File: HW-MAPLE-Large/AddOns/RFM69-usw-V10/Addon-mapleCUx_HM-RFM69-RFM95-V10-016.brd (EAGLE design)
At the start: 49 x 47 mm, 35 parts, among them IC1 ATSHA204A, IC31 ATMEGA168-TQFP, X31 M03X2, X4 1751248, X7 1751264, Y2 8MHZ

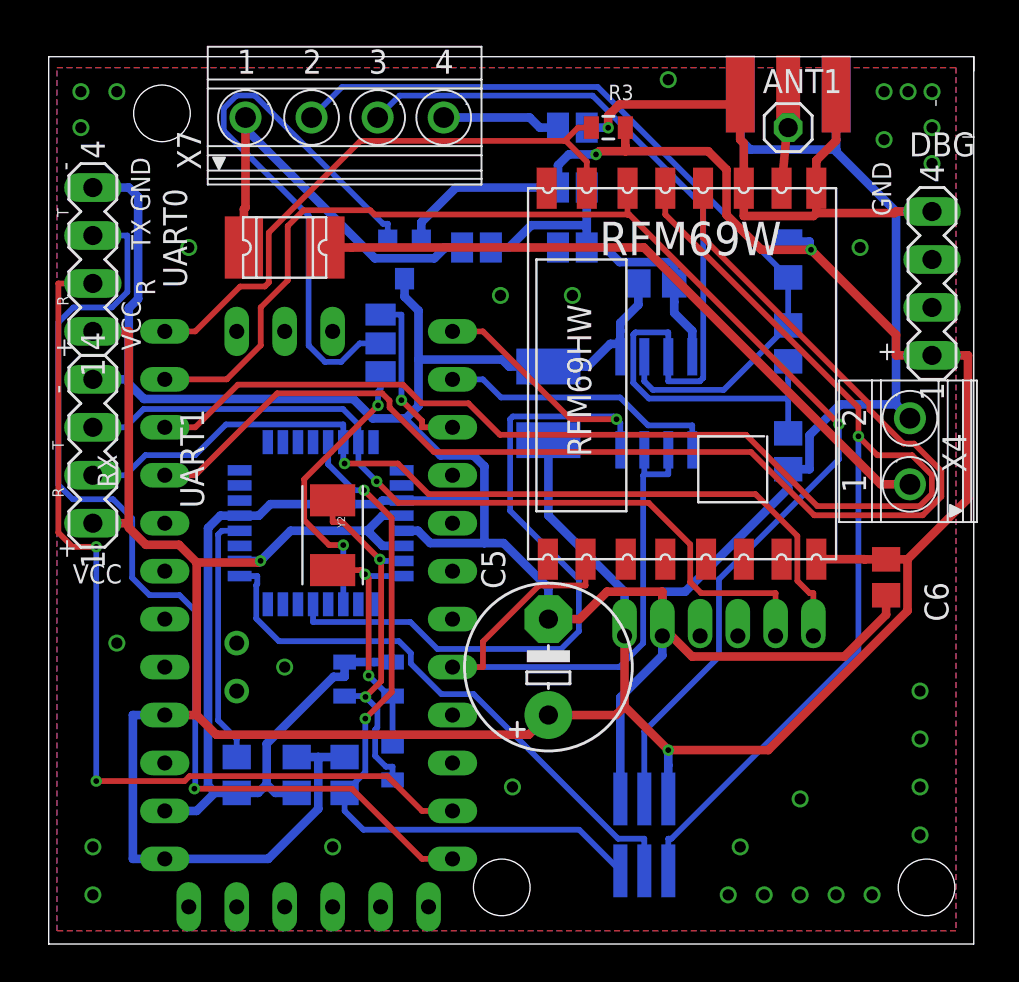
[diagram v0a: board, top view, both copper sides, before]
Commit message: Addon: plus RFM95
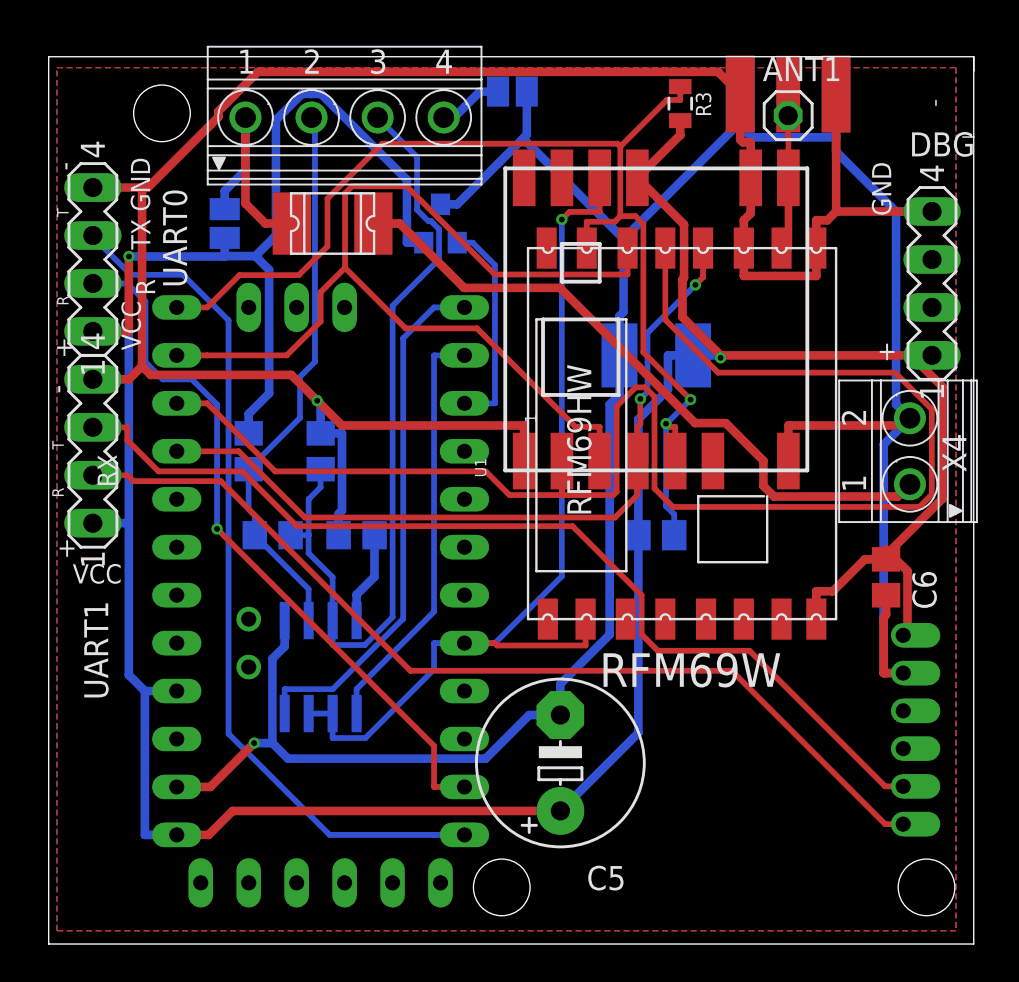
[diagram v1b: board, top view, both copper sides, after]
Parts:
- removed 3V3, 5V: (no value), jumper:SJ
- removed C14, C15: 30pf, doug:0805
- removed C31, C32: 100n, rcl:C0805
- removed IC31: ATMEGA168-TQFP, atmel:TQFP32-08
- removed R34: (no value), rcl:R0805
- removed R4: 1M, doug:0805
- removed SJ1: (no value), jumper:SJ_2
- removed X31: M03X2, mechanics:2X03-1.27MM_SMD
- removed Y2: 8MHZ, SparkFun-FreqCtrl:CRYSTAL-TXC-7A
- added R2: 10k, rcl:M0805
- added U1: RFM69HCW, doug:RFM69HCW-XXXS2
- moved R9 30.3 mm to (61.6, 38.1)
- moved R1 29.1 mm to (62.9, 33.7), turned to 180 degrees
- moved R10 24.8 mm to (65.4, 38.1), turned to 90 degrees
- moved RS1 22.6 mm to (65.4, 26.7)
- moved C10 20.7 mm to (67.3, 33.7)
- moved EXT 13.4 mm to (60.3, 50.2), turned to 90 degrees
- moved HMMOD-UART 12.3 mm to (96.3, 16.4), turned to 0 degrees
- moved C7 6.25 mm to (83.2, 43.2), turned to 180 degrees
- moved C5 5.12 mm to (78.1, 21.6)
- moved R3 4.02 mm to (84.5, 56.5), turned to 270 degrees
- moved GND 3.70 mm to (75.6, 57.1)
- moved RFM69W 3.17 mm to (92.7, 29.2)
- moved F1 2.84 mm to (66.0, 50.2)
- moved IC1 2.69 mm to (71.8, 50.2), turned to 0 degrees
- moved U$2 1.42 mm to (67.9, 24.1)
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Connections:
- removed net +5V: 5V.2
- removed net D10_SS: IC31.14
- removed net D11_MOSI: IC31.15
- removed net D12_MISO: IC31.16
- removed net D13_SCK: IC31.17, X31.P$3
- removed net D2_INT0: IC31.32
- removed net D7-ATSHA-MEGA: IC31.11, SJ1.1
- removed net M-RES: IC31.29, R34.2, X31.P$5
- removed net N$1: ANT1.1, RFM69W.ANT, X2.P
- removed net N$13: C32.1, IC31.20
- removed net N$19: C15.2, IC31.8, R4.1, Y2.P$1
- removed net N$3: C14.2, IC31.7, R4.2, Y2.P$2
- removed net N$5: IC1.1, SJ1.2
- new net ANT: ANT1.1, RFM69W.ANT, U1.ANT, X2.P
- new net N$14: U1.DIO2
- new net N$15: U1.DIO1
- new net N$2: U1.RESET
- net CE-A: no longer IC31.13
- net CSN-A: now also R2.1, U1.NSS
- net D7-ATSHA-ARDU: now also IC1.1; no longer SJ1.3
- net GND: now also U1.GND_1, U1.GND_2, U1.GND_3; no longer C14.1, C15.1, C31.2, C32.2, IC31.21, IC31.3, IC31.5, X31.P$6
- net IRQ-A: now also U1.DIO0
- net MISO-A: now also U1.MISO; no longer X31.P$1
- net MOSI-A: now also U1.MOSI; no longer X31.P$4
- net RX1: no longer IC31.31
- net SCK-A: now also U1.SCK
- net TX1: no longer IC31.30
- net VCC: now also EXT.1, R2.2, U1.3.3V; no longer 3V3.1, C31.1, IC31.18, IC31.4, IC31.6, R34.1, X31.P$2
- net VDD: no longer 3V3.2, 5V.1, EXT.1
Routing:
- net M-RES: track 38.2 -> 0.00 mm, vias 2 -> 0
- net N$5: track 31.7 -> 0.00 mm
- net CSN-A: track 31.6 -> 62.5 mm, vias 0 -> 2
- net D13_SCK: track 30.6 -> 0.00 mm
- net SCK-A: track 68.1 -> 40.9 mm, vias 0 -> 2
- net N$3: track 19.7 -> 0.00 mm, vias 2 -> 0
- net MOSI-A: track 72.5 -> 52.9 mm, vias 1 -> 0
- net CE-A: track 46.8 -> 27.9 mm, vias 1 -> 0
- net MISO-A: track 94.9 -> 79.0 mm, vias 1 -> 0
- net IRQ-A: track 34.5 -> 49.8 mm, vias 0 -> 1
- net D7-ATSHA-MEGA: track 15.3 -> 0.00 mm, vias 2 -> 0
- net VDD: track 19.1 -> 4.91 mm
- net 1W: track 43.2 -> 29.5 mm
- net N$19: track 13.6 -> 0.00 mm, vias 2 -> 0
- net N$13: track 13.4 -> 0.00 mm
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
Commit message: Update RFM95, etc.
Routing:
- net GND: vias 2 -> 29
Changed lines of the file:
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@@
 <wire x1="97.79" y1="50.8" x2="95.8849" y2="50.8" width="0.4572" layer="16"/>
 <wire x1="92.71" y1="57.023" x2="92.71" y2="54.7319" width="0.4572" layer="16"/>
+<via x="53.975" y="14.605" extent="1-16" drill="0.6" shape="square"/>
+<via x="53.975" y="17.78" extent="1-16" drill="0.6" shape="square"/>
+<via x="53.975" y="20.955" extent="1-16" drill="0.6" shape="square"/>
+<via x="53.975" y="24.765" extent="1-16" drill="0.6" shape="square"/>
+<via x="53.975" y="28.575" extent="1-16" drill="0.6" shape="square"/>
+<via x="53.34" y="55.245" extent="1-16" drill="0.6" shape="square"/>
+<via x="53.34" y="57.15" extent="1-16" drill="0.6" shape="square"/>
+<via x="54.61" y="57.15" extent="1-16" drill="0.6" shape="square"/>
+<via x="57.785" y="50.8" extent="1-16" drill="0.6" shape="square"/>
+<via x="67.945" y="41.91" extent="1-16" drill="0.6" shape="square"/>
+<via x="67.945" y="20.32" extent="1-16" drill="0.6" shape="square"/>
+<via x="76.2" y="21.59" extent="1-16" drill="0.6" shape="square"/>
+<via x="82.55" y="13.97" extent="1-16" drill="0.6" shape="square"/>
+<via x="94.615" y="13.97" extent="1-16" drill="0.6" shape="square"/>
+<via x="91.44" y="13.97" extent="1-16" drill="0.6" shape="square"/>
+<via x="88.9" y="13.97" extent="1-16" drill="0.6" shape="square"/>
+<via x="85.725" y="13.97" extent="1-16" drill="0.6" shape="square"/>
+<via x="86.36" y="23.495" extent="1-16" drill="0.6" shape="square"/>
+<via x="90.17" y="33.02" extent="1-16" drill="0.6" shape="square"/>
+<via x="88.9" y="40.64" extent="1-16" drill="0.6" shape="square"/>
+<via x="89.535" y="45.085" extent="1-16" drill="0.6" shape="square"/>
+<via x="80.01" y="56.515" extent="1-16" drill="0.6" shape="square"/>
+<via x="95.885" y="56.515" extent="1-16" drill="0.6" shape="square"/>
+<via x="97.155" y="55.245" extent="1-16" drill="0.6" shape="square"/>
+<via x="95.25" y="54.61" extent="1-16" drill="0.6" shape="square"/>
+<via x="93.98" y="46.355" extent="1-16" drill="0.6" shape="square"/>
+<via x="97.79" y="31.75" extent="1-16" drill="0.6" shape="square"/>
 </signal>
 <signal name="VCC" class="1">
